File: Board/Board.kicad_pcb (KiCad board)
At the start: 2 copper layers, 45 x 22.7 mm, 41 parts, among them J1 5025700893, J2 Conn_01x02_Male, Q1 Q_NMOS_GSD, Q2 Q_NMOS_GSD, SW2 SW_SPST, U1 ATmega328P-AU, U2 TLV61225DCKR, Y1 10MHz

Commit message: Board done :)
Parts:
- added G***: LOGO, Board:logo, B.Cu at (44.2, 39.6)

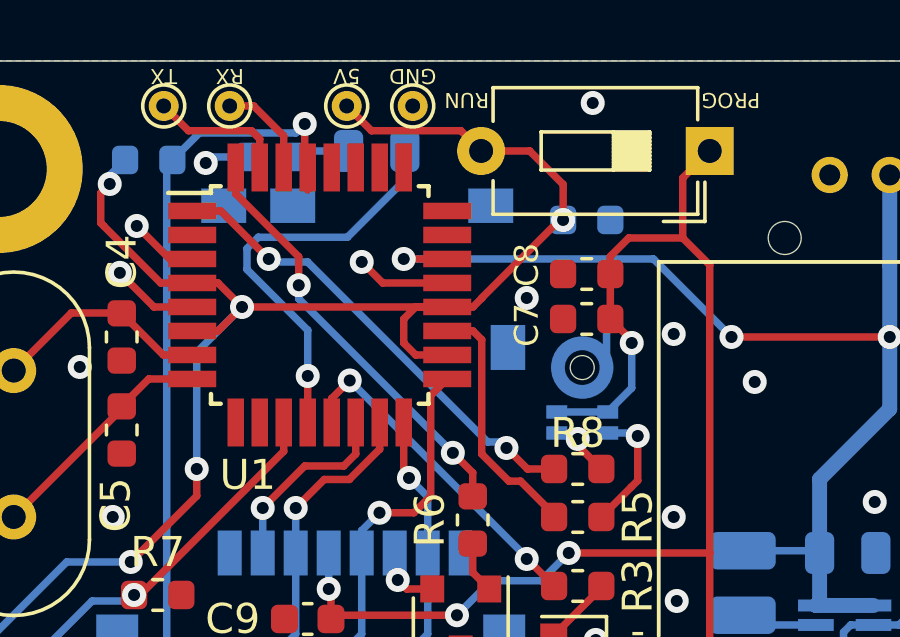
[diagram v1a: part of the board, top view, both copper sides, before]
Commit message: Board V1.1: ARef fix
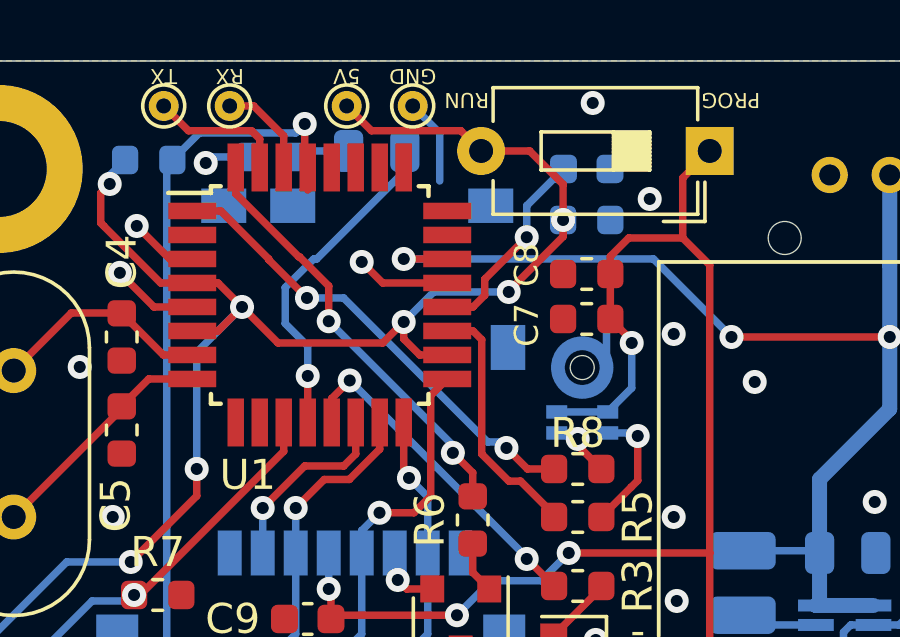
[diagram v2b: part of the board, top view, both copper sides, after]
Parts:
- added C10: 100nF, Capacitor_SMD:C_0603_1608Metric, B.Cu at (43.2, 23.6)
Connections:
- U1 pad 20: MCU_POWER -> Net-(C10-Pad1)
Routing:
- net Net-(C10-Pad1): track 0.00 -> 6.71 mm, vias 0 -> 1
- net GND: track 11.8 -> 14.6 mm
- net Net-(D1-Pad2): track 13.8 -> 11.1 mm
- net MCU_POWER: track 53.6 -> 53.2 mm, vias 5 -> 7

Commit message: Minor improvements
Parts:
- removed C4, C5: 18pF, Capacitor_SMD:C_0603_1608Metric
- removed the G*** at (44.2, 39.6)
- removed R4: 3.48, Resistor_SMD:R_2512_6332Metric
- removed Y1: 10MHz, Crystal:Crystal_HC49-4H_Vertical
- added G***: LOGO, Board:Logo, F.Cu at (24.8, 30.8)
- TP1, TP10, TP2, TP3, TP4, TP5, TP6, TP7, TP8, TP9: footprint TestPoint:TestPoint_THTPad_D1.0mm_Drill0.5mm -> Board:TestPoint_THTPad_D1.0mm_Drill0.7mm
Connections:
- C6 pad 1: +3V3 -> +BATT
- LS1 pad 1: Net-(LS1-Pad1) -> +BATT
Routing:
- net +BATT: track 38.6 -> 53.8 mm, vias 3 -> 4
- net +3V3: track 59.3 -> 50.3 mm
- net Net-(U1-Pad8): track 7.91 -> 0.00 mm
- net Net-(U1-Pad7): track 7.33 -> 0.00 mm
- net Net-(LS1-Pad1): track 0.40 -> 0.00 mm, vias 1 -> 0
- net GND: track 14.6 -> 14.5 mm, vias 20 -> 21

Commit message: New microphone circuit
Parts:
- added C4: 100nF, Capacitor_SMD:C_0603_1608Metric, F.Cu at (46.3, 13.2)
- added MK1: ICS-40181, Board:MIC_ICS-40181, F.Cu at (14.1, 32.3)
- added MK2: CMM-3526AB-38308-TR, Board:XDCR_CMM-3526AB-38308-TR, B.Cu at (51.6, 13.4)
- added U3: MCP6001UT-I_OT, Board:SOT95P270X145-5N, F.Cu at (8.56, 32.2)
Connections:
- U1 pad 1: /MICCLK -> Net-(U1-Pad1)
- U1 pad 19: /MICDATA -> Net-(U1-Pad19)

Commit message: PCB v1.1 done
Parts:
- removed C7, C8: 100nF, Capacitor_SMD:C_0603_1608Metric
- removed the MK1 at (43.0, 30.9)
- removed the MK1 at (14.1, 32.3)
- removed MK2: CMM-3526AB-38308-TR, Board:XDCR_CMM-3526AB-38308-TR
- removed R5: 68, Resistor_SMD:R_0603_1608Metric
- added C5: 4.7uF, Capacitor_SMD:C_0603_1608Metric, F.Cu at (22.7, 32.4)
- added MK1: ICS-40181, Board:MIC_ICS-40181, F.Cu at (23.3, 29.6)
- added R10: 510, Resistor_SMD:R_0603_1608Metric, F.Cu at (22.7, 37.7)
- added R11: 10K, Resistor_SMD:R_0603_1608Metric, F.Cu at (42.6, 24.8)
- added R12: 10K, Resistor_SMD:R_0603_1608Metric, F.Cu at (42.6, 29.9)
- added R13: 10K, Resistor_SMD:R_0603_1608Metric, F.Cu at (42.6, 26.5)
- added R14: 10K, Resistor_SMD:R_0603_1608Metric, F.Cu at (42.6, 28.2)
- added R4: 21K, Resistor_SMD:R_0603_1608Metric, F.Cu at (29.5, 36.4)
- added R9: 10K, Resistor_SMD:R_0603_1608Metric, F.Cu at (22.7, 35.9)
- C1, D1, R2: moved to F.Cu
- G***, R7: moved to B.Cu
- R8: value 68 -> 10K
- moved C4 25.6 mm to (26.9, 29.9)
- moved TP9 20.5 mm to (22.8, 40.2)
- moved R8 20.2 mm to (22.7, 34.3), turned to 0 degrees
- moved TP8 19.9 mm to (30.7, 40.2)
- moved TP10 19.1 mm to (25.2, 40.2)
- moved TP4 19.0 mm to (30.0, 22.5)
- moved TP6 19.0 mm to (27.8, 22.5)
- moved TP5 19.0 mm to (32.2, 22.5)
- moved TP3 18.8 mm to (33.1, 40.2)
- moved C9 18.0 mm to (41.9, 22.5), turned to 90 degrees
- moved U3 17.8 mm to (26.3, 34.0), turned to 90 degrees
- moved SW2 17.5 mm to (43.1, 40.0)
- moved C10 17.3 mm to (38.9, 40.4), turned to 270 degrees
- moved Q2 17.0 mm to (46.3, 23.3), turned to 180 degrees
- moved TP1 16.4 mm to (27.8, 25.5)
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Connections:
- C4 pad 1: GND -> +3V3
- C4 pad 2: +3V3 -> GND
- D1 pad 2: Net-(D1-Pad2) -> /LED
- Q1 pad 2: Net-(LS1-Pad2) -> GND
- Q1 pad 3: GND -> Net-(LS1-Pad2)
- Q2 pad 2: Net-(J1-Pad6) -> GND
- Q2 pad 3: GND -> Net-(J1-Pad6)
- R8 pad 1: Net-(MK1-Pad3) -> +3V3
- R8 pad 2: /MICCLK -> Net-(R8-Pad2)
- U1 pad 12: Net-(D1-Pad2) -> Net-(U1-Pad12)
- U1 pad 23: Net-(U1-Pad23) -> /LED
- U1 pad 26: Net-(U1-Pad26) -> /MICDATA
- U1 pad 32: /SD_POWER -> Net-(U1-Pad32)
- U1 pad 9: Net-(U1-Pad9) -> /SD_POWER
- U3 pad 1: Net-(U3-Pad1) -> Net-(R8-Pad2)
- U3 pad 2: Net-(U3-Pad2) -> GND
- U3 pad 4: Net-(U3-Pad4) -> /MICDATA
- U3 pad 5: Net-(U3-Pad5) -> +3V3
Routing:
- net MCU_POWER: track 52.9 -> 32.1 mm, vias 7 -> 1
- net +3V3: track 50.3 -> 69.8 mm, vias 5 -> 2
- net /MICCLK: track 16.0 -> 0.00 mm, vias 2 -> 0
- net /RESET: track 25.1 -> 12.2 mm
- net Net-(D1-Pad2): track 11.1 -> 0.00 mm, vias 1 -> 0
- net Net-(TP9-Pad1): track 3.26 -> 12.2 mm, vias 0 -> 1
- net Net-(R10-Pad2): track 0.00 -> 8.56 mm
- net /MOSI: track 11.7 -> 20.1 mm, vias 1 -> 3
- net Net-(J1-Pad6): track 2.22 -> 10.4 mm
- net /SPEAKER: track 11.5 -> 3.51 mm, vias 2 -> 0
- net Net-(C10-Pad1): track 6.71 -> 14.6 mm
- net Net-(J1-Pad8): track 0.00 -> 7.56 mm, vias 0 -> 1
- net Net-(C5-Pad2): track 0.00 -> 7.23 mm
- net +BATT: track 53.8 -> 60.7 mm, vias 4 -> 2
- net /LED: track 0.00 -> 5.90 mm, vias 0 -> 2
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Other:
- board text added: "GND|BATT"
- board text added: "RUN|PROG"
- board text added: "SWITCH"
- board text removed: "GND/BATT"
- board text removed: "PROG"
- board text removed: "RUN"
- board text removed: "SW+"
- board text removed: "SW-"

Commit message: PCB v1.1 ready
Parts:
- C10: moved to F.Cu
- moved C10 16.2 mm to (34.8, 24.7), turned to 180 degrees
- moved C4 0.80 mm to (26.9, 30.7)
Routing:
- net Net-(C10-Pad1): track 14.6 -> 2.08 mm, vias 1 -> 0
- net +BATT: track 60.7 -> 57.1 mm
- net +3V3: track 69.8 -> 71.6 mm, vias 2 -> 4
- net GND: track 19.5 -> 21.1 mm, vias 28 -> 29
- net /MOSI: track 20.1 -> 18.9 mm, vias 3 -> 2
- net Net-(R7-Pad1): track 12.3 -> 12.8 mm
- net /MISO: track 14.4 -> 15.0 mm

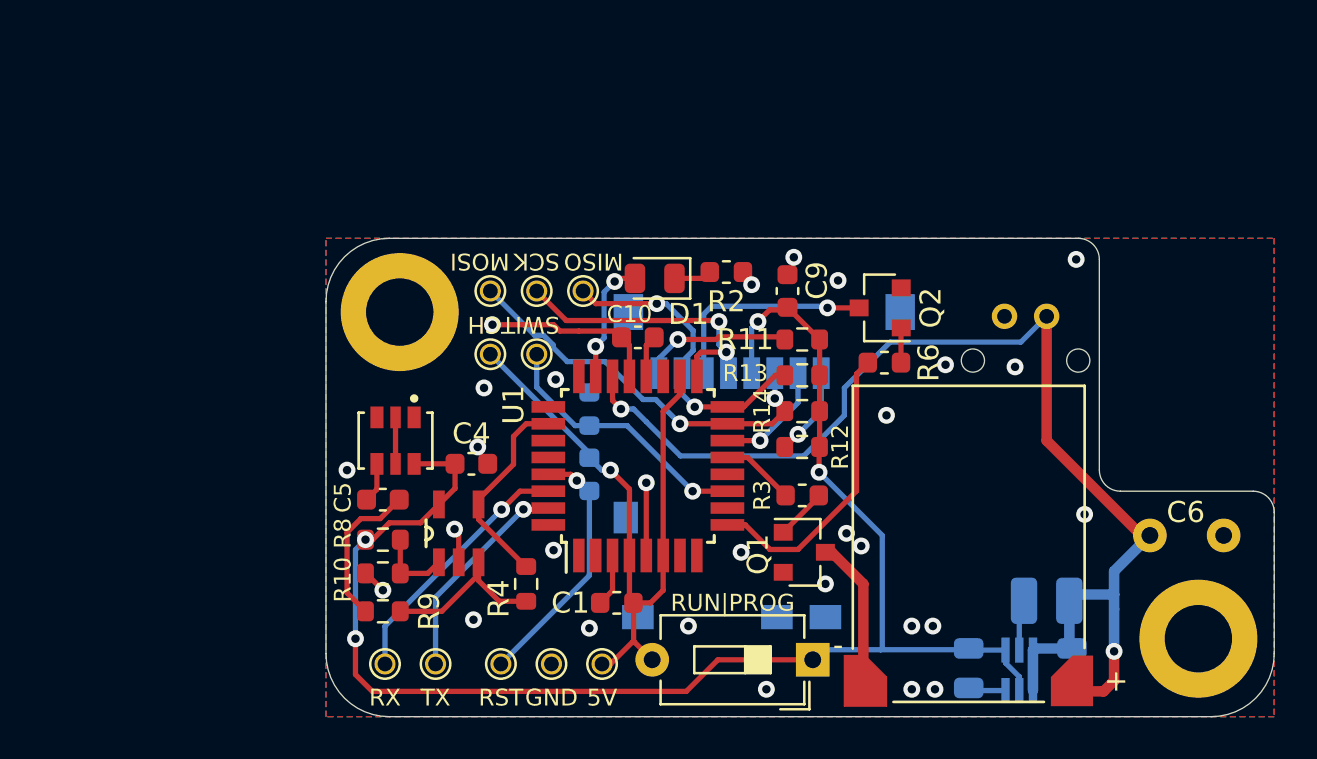
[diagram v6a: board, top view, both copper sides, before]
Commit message: Added Gate pulldowns
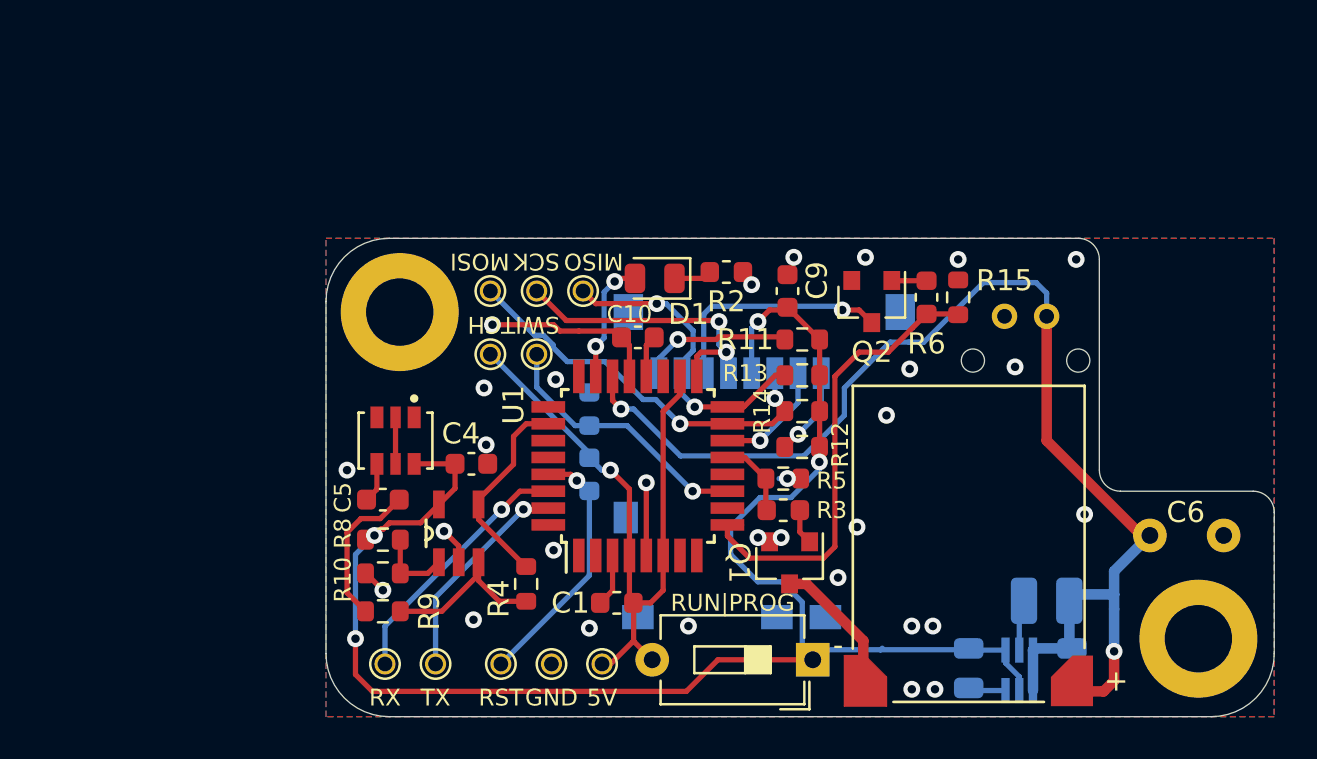
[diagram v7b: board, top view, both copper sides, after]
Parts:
- added R15: 10K, Resistor_SMD:R_0603_1608Metric, F.Cu at (50.0, 22.8)
- added R5: 10K, Resistor_SMD:R_0603_1608Metric, F.Cu at (41.7, 31.4)
- moved R6 3.69 mm to (48.5, 22.8), turned to 270 degrees
- moved R3 1.14 mm to (41.7, 32.9)
- moved Q1 0.86 mm to (42.0, 35.4), turned to 270 degrees
- moved Q2 0.50 mm to (45.9, 23.0), turned to 270 degrees
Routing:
- net /SD_POWER: track 14.1 -> 22.1 mm
- net +3V3: track 71.6 -> 76.9 mm
- net +BATT: track 57.1 -> 59.1 mm
- net GND: track 21.1 -> 22.3 mm, vias 29 -> 30
- net Net-(J1-Pad6): track 10.4 -> 11.3 mm
- net Net-(Q1-Pad1): track 2.45 -> 1.69 mm
- net Net-(LS1-Pad2): track 7.51 -> 7.01 mm
